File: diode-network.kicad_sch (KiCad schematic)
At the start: 16 parts

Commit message: add pss 3dmodels and testpoints
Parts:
- JP29001, JP29002, JP29003, JP29005: footprint (none) -> Jumper:SolderJumper-2_P1.3mm_Open_RoundedPad1.0x1.5mm
- JP29004, JP29006, JP29007, JP29008: footprint (none) -> pss:SolderJumper-2_P1.3mm_Bridged-Soldermask-Paste_RoundedPad1.0x1.5mm
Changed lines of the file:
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@@
 			)
 		)
-		(property "Footprint" ""
+		(property "Footprint" "pss:SolderJumper-2_P1.3mm_Bridged-Soldermask-Paste_RoundedPad1.0x1.5mm"
 			(at 171.45 101.6 0)
 			(effects
@@
 			)
 		)
-		(property "Footprint" ""
+		(property "Footprint" "Jumper:SolderJumper-2_P1.3mm_Open_RoundedPad1.0x1.5mm"
 			(at 146.05 101.6 0)
 			(effects
@@
 			)
 		)
-		(property "Footprint" ""
+		(property "Footprint" "Jumper:SolderJumper-2_P1.3mm_Open_RoundedPad1.0x1.5mm"
 			(at 133.35 127 0)
 			(effects
@@
 			)
 		)
-		(property "Footprint" ""
+		(property "Footprint" "Jumper:SolderJumper-2_P1.3mm_Open_RoundedPad1.0x1.5mm"
 			(at 158.75 101.6 0)
 			(effects
@@
 			)
 		)
-		(property "Footprint" ""
+		(property "Footprint" "Jumper:SolderJumper-2_P1.3mm_Open_RoundedPad1.0x1.5mm"
 			(at 133.35 101.6 0)
 			(effects
@@
 			)
 		)
-		(property "Footprint" ""
+		(property "Footprint" "pss:SolderJumper-2_P1.3mm_Bridged-Soldermask-Paste_RoundedPad1.0x1.5mm"
 			(at 158.75 127 0)
 			(effects
@@
 			)
 		)
-		(property "Footprint" ""
+		(property "Footprint" "pss:SolderJumper-2_P1.3mm_Bridged-Soldermask-Paste_RoundedPad1.0x1.5mm"
 			(at 146.05 127 0)
 			(effects
@@
 			)
 		)
-		(property "Footprint" ""
+		(property "Footprint" "pss:SolderJumper-2_P1.3mm_Bridged-Soldermask-Paste_RoundedPad1.0x1.5mm"
 			(at 171.45 127 0)
 			(effects

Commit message: edit pss symbol library: export all schematic symbols to library 'pss' and update symbol link
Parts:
- D29001, D29002, D29003, D29004, D29005, D29006, D29007, D29008: symbol Device:D -> pss:D
- JP29001, JP29002, JP29003, JP29005: symbol Jumper:SolderJumper_2_Open -> pss:SolderJumper_2_Open
- JP29004, JP29006, JP29007, JP29008: symbol Jumper:SolderJumper_2_Bridged -> pss:SolderJumper_2_Bridged
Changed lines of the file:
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@@
 	)
 	(symbol
-		(lib_id "Jumper:SolderJumper_2_Bridged")
+		(lib_id "pss:SolderJumper_2_Bridged")
 		(at 171.45 101.6 0)
 		(unit 1)
@@
 	)
 	(symbol
-		(lib_id "Device:D")
+		(lib_id "pss:D")
 		(at 171.45 88.9 180)
 		(unit 1)
@@
 	)
 	(symbol
-		(lib_id "Device:D")
+		(lib_id "pss:D")
 		(at 133.35 114.3 0)
 		(unit 1)
@@
 	)
 	(symbol
-		(lib_id "Device:D")
+		(lib_id "pss:D")
 		(at 133.35 88.9 180)
 		(unit 1)
@@
 	)
 	(symbol
-		(lib_id "Device:D")
+		(lib_id "pss:D")
 		(at 146.05 114.3 0)
 		(unit 1)
@@
 	)
 	(symbol
-		(lib_id "Jumper:SolderJumper_2_Open")
+		(lib_id "pss:SolderJumper_2_Open")
 		(at 146.05 101.6 0)
 		(unit 1)
@@
 	)
 	(symbol
-		(lib_id "Jumper:SolderJumper_2_Open")
+		(lib_id "pss:SolderJumper_2_Open")
 		(at 133.35 127 0)
 		(unit 1)
@@
 	)
 	(symbol
-		(lib_id "Jumper:SolderJumper_2_Open")
+		(lib_id "pss:SolderJumper_2_Open")
 		(at 158.75 101.6 0)
 		(unit 1)
@@
 	)
 	(symbol
-		(lib_id "Jumper:SolderJumper_2_Open")
+		(lib_id "pss:SolderJumper_2_Open")
 		(at 133.35 101.6 0)
 		(unit 1)
@@
 	)
 	(symbol
-		(lib_id "Device:D")
+		(lib_id "pss:D")
 		(at 158.75 114.3 0)
 		(unit 1)
@@
 	)
 	(symbol
-		(lib_id "Device:D")
+		(lib_id "pss:D")
 		(at 171.45 114.3 0)
 		(unit 1)
@@
 	)
 	(symbol
-		(lib_id "Jumper:SolderJumper_2_Bridged")
+		(lib_id "pss:SolderJumper_2_Bridged")
 		(at 158.75 127 0)
 		(unit 1)
@@
 	)
 	(symbol
-		(lib_id "Jumper:SolderJumper_2_Bridged")
+		(lib_id "pss:SolderJumper_2_Bridged")
 		(at 146.05 127 0)
 		(unit 1)
@@
 	)
 	(symbol
-		(lib_id "Device:D")
+		(lib_id "pss:D")
 		(at 146.05 88.9 180)
 		(unit 1)
@@
 	)
 	(symbol
-		(lib_id "Jumper:SolderJumper_2_Bridged")
+		(lib_id "pss:SolderJumper_2_Bridged")
 		(at 171.45 127 0)
 		(unit 1)
@@
 	)
 	(symbol
-		(lib_id "Device:D")
+		(lib_id "pss:D")
 		(at 158.75 88.9 180)
 		(unit 1)

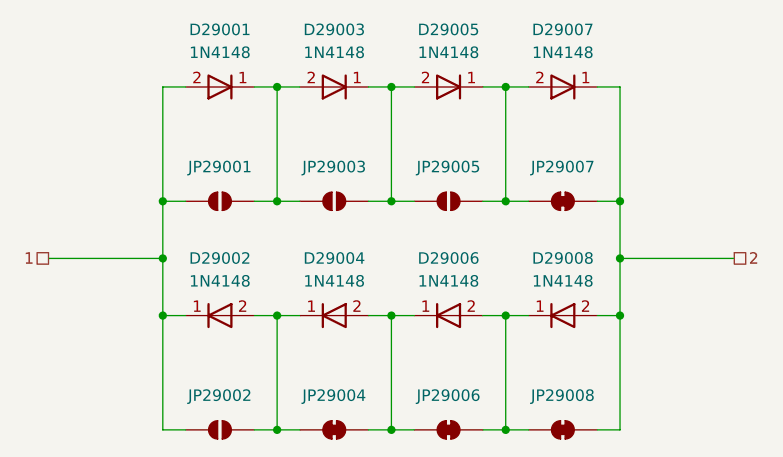
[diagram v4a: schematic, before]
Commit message: edit pss footprint library: export all footprints to library 'pss' and update footprint links
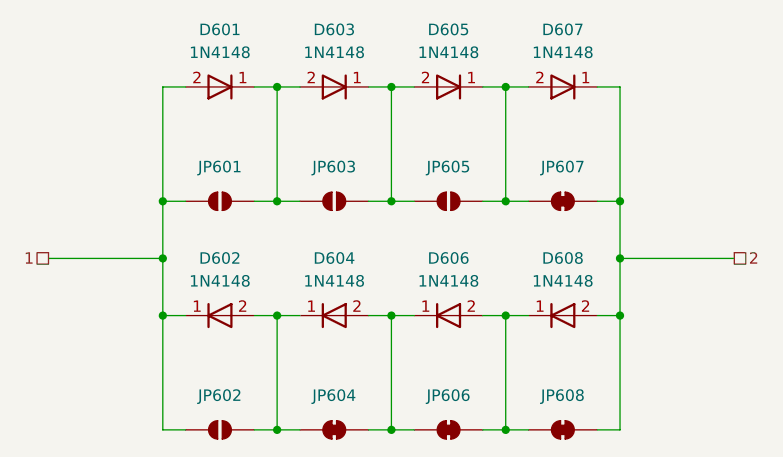
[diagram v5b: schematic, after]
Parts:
- D601: renamed from D29001; footprint Diode_SMD:D_SOD-123 -> pss:D_SOD-123
- D602: renamed from D29002; footprint Diode_SMD:D_SOD-123 -> pss:D_SOD-123
- D603: renamed from D29003; footprint Diode_SMD:D_SOD-123 -> pss:D_SOD-123
- D604: renamed from D29004; footprint Diode_SMD:D_SOD-123 -> pss:D_SOD-123
- D605: renamed from D29005; footprint Diode_SMD:D_SOD-123 -> pss:D_SOD-123
- D606: renamed from D29006; footprint Diode_SMD:D_SOD-123 -> pss:D_SOD-123
- D607: renamed from D29007; footprint Diode_SMD:D_SOD-123 -> pss:D_SOD-123
- D608: renamed from D29008; footprint Diode_SMD:D_SOD-123 -> pss:D_SOD-123
- JP601: renamed from JP29001; footprint Jumper:SolderJumper-2_P1.3mm_Open_RoundedPad1.0x1.5mm -> pss:SolderJumper-2_P1.3mm_Open_RoundedPad1.0x1.5mm
- JP602: renamed from JP29002; footprint Jumper:SolderJumper-2_P1.3mm_Open_RoundedPad1.0x1.5mm -> pss:SolderJumper-2_P1.3mm_Open_RoundedPad1.0x1.5mm
- JP603: renamed from JP29003; footprint Jumper:SolderJumper-2_P1.3mm_Open_RoundedPad1.0x1.5mm -> pss:SolderJumper-2_P1.3mm_Open_RoundedPad1.0x1.5mm
- JP605: renamed from JP29005; footprint Jumper:SolderJumper-2_P1.3mm_Open_RoundedPad1.0x1.5mm -> pss:SolderJumper-2_P1.3mm_Open_RoundedPad1.0x1.5mm
- renumbered JP29004 to JP604, JP29006 to JP606, JP29007 to JP607, JP29008 to JP608
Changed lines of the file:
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@@
 		(on_board yes)
 		(dnp no)
-		(property "Reference" "JP29007"
+		(property "Reference" "JP607"
 			(at 171.45 97.79 0)
 			(effects
@@
 		(dnp no)
 		(fields_autoplaced yes)
-		(property "Reference" "D29007"
+		(property "Reference" "D607"
 			(at 171.45 82.55 0)
 			(effects
@@
 			)
 		)
-		(property "Footprint" "Diode_SMD:D_SOD-123"
+		(property "Footprint" "pss:D_SOD-123"
 			(at 171.45 88.9 0)
 			(effects
@@
 		(dnp no)
 		(fields_autoplaced yes)
-		(property "Reference" "D29002"
+		(property "Reference" "D602"
 			(at 133.35 107.95 0)
 			(effects
@@
 			)
 		)
-		(property "Footprint" "Diode_SMD:D_SOD-123"
+		(property "Footprint" "pss:D_SOD-123"
 			(at 133.35 114.3 0)
 			(effects
@@
 		(dnp no)
 		(fields_autoplaced yes)
-		(property "Reference" "D29001"
+		(property "Reference" "D601"
 			(at 133.35 82.55 0)
 			(effects
@@
 			)
 		)
-		(property "Footprint" "Diode_SMD:D_SOD-123"
+		(property "Footprint" "pss:D_SOD-123"
 			(at 133.35 88.9 0)
 			(effects
@@
 		(dnp no)
 		(fields_autoplaced yes)
-		(property "Reference" "D29004"
+		(property "Reference" "D604"
 			(at 146.05 107.95 0)
 			(effects
@@
 			)
 		)
-		(property "Footprint" "Diode_SMD:D_SOD-123"
+		(property "Footprint" "pss:D_SOD-123"
 			(at 146.05 114.3 0)
 			(effects
@@
 		(on_board yes)
 		(dnp no)
-		(property "Reference" "JP29003"
+		(property "Reference" "JP603"
 			(at 146.05 97.79 0)
 			(effects
@@
 			)
 		)
-		(property "Footprint" "Jumper:SolderJumper-2_P1.3mm_Open_RoundedPad1.0x1.5mm"
+		(property "Footprint" "pss:SolderJumper-2_P1.3mm_Open_RoundedPad1.0x1.5mm"
 			(at 146.05 101.6 0)
 			(effects
@@
 		(on_board yes)
 		(dnp no)
-		(property "Reference" "JP29002"
+		(property "Reference" "JP602"
 			(at 133.35 123.19 0)
 			(effects
@@
 			)
 		)
-		(property "Footprint" "Jumper:SolderJumper-2_P1.3mm_Open_RoundedPad1.0x1.5mm"
+		(property "Footprint" "pss:SolderJumper-2_P1.3mm_Open_RoundedPad1.0x1.5mm"
 			(at 133.35 127 0)
 			(effects
@@
 		(on_board yes)
 		(dnp no)
-		(property "Reference" "JP29005"
+		(property "Reference" "JP605"
 			(at 158.75 97.79 0)
 			(effects
@@
 			)
 		)
-		(property "Footprint" "Jumper:SolderJumper-2_P1.3mm_Open_RoundedPad1.0x1.5mm"
+		(property "Footprint" "pss:SolderJumper-2_P1.3mm_Open_RoundedPad1.0x1.5mm"
 			(at 158.75 101.6 0)
 			(effects
@@
 		(on_board yes)
 		(dnp no)
-		(property "Reference" "JP29001"
+		(property "Reference" "JP601"
 			(at 133.35 97.79 0)
 			(effects
@@
 			)
 		)
-		(property "Footprint" "Jumper:SolderJumper-2_P1.3mm_Open_RoundedPad1.0x1.5mm"
+		(property "Footprint" "pss:SolderJumper-2_P1.3mm_Open_RoundedPad1.0x1.5mm"
 			(at 133.35 101.6 0)
 			(effects
@@
 		(dnp no)
 		(fields_autoplaced yes)
-		(property "Reference" "D29006"
+		(property "Reference" "D606"
 			(at 158.75 107.95 0)
 			(effects
@@
 			)
 		)
-		(property "Footprint" "Diode_SMD:D_SOD-123"
+		(property "Footprint" "pss:D_SOD-123"
 			(at 158.75 114.3 0)
 			(effects
@@
 		(dnp no)
 		(fields_autoplaced yes)
-		(property "Reference" "D29008"
+		(property "Reference" "D608"
 			(at 171.45 107.95 0)
 			(effects
@@
 			)
 		)
-		(property "Footprint" "Diode_SMD:D_SOD-123"
+		(property "Footprint" "pss:D_SOD-123"
 			(at 171.45 114.3 0)
 			(effects
@@
 		(on_board yes)
 		(dnp no)
-		(property "Reference" "JP29006"
+		(property "Reference" "JP606"
 			(at 158.75 123.19 0)
 			(effects
@@
 		(on_board yes)
 		(dnp no)
-		(property "Reference" "JP29004"
+		(property "Reference" "JP604"
 			(at 146.05 123.19 0)
 			(effects
@@
 		(dnp no)
 		(fields_autoplaced yes)
-		(property "Reference" "D29003"
+		(property "Reference" "D603"
 			(at 146.05 82.55 0)
 			(effects
@@
 			)
 		)
-		(property "Footprint" "Diode_SMD:D_SOD-123"
+		(property "Footprint" "pss:D_SOD-123"
 			(at 146.05 88.9 0)
 			(effects
@@
 		(on_board yes)
 		(dnp no)
-		(property "Reference" "JP29008"
+		(property "Reference" "JP608"
 			(at 171.45 123.19 0)
 			(effects
@@
 		(dnp no)
 		(fields_autoplaced yes)
-		(property "Reference" "D29005"
+		(property "Reference" "D605"
 			(at 158.75 82.55 0)
 			(effects
@@
 			)
 		)
-		(property "Footprint" "Diode_SMD:D_SOD-123"
+		(property "Footprint" "pss:D_SOD-123"
 			(at 158.75 88.9 0)
 			(effects
